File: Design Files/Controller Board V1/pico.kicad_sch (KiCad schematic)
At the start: 1 part, among them U5 SC0917

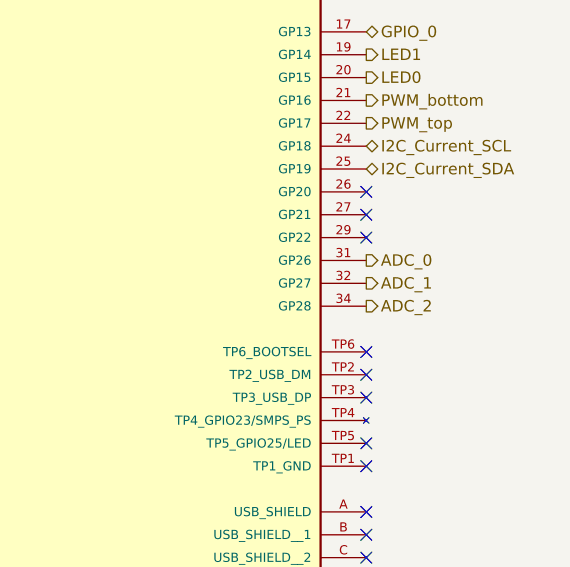
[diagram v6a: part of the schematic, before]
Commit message: current sensor done
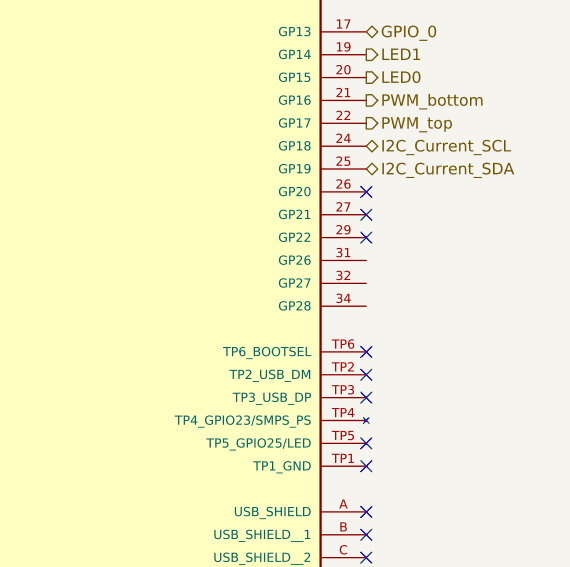
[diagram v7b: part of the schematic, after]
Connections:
- net ADC_0: no longer names the net of U5.31 (GP26)
- net ADC_1: no longer names the net of U5.32 (GP27)
- net ADC_2: no longer names the net of U5.34 (GP28)
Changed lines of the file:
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@@
 		(shape bidirectional)
 		(at 107.95 81.28 180)
-		(fields_autoplaced yes)
 		(effects
 			(font
@@
 		(shape bidirectional)
 		(at 107.95 91.44 180)
-		(fields_autoplaced yes)
-		(effects
-			(font
-				(size 1.27 1.27)
-			)
-			(justify right)
-		)
-	)
-	(hierarchical_label "ADC_1"
-		(shape output)
-		(at 158.75 96.52 0)
-		(fields_autoplaced yes)
-		(effects
-			(font
-				(size 1.27 1.27)
-			)
-			(justify left)
+		(effects
+			(font
+				(size 1.27 1.27)
+			)
+			(justify right)
 		)
 	)
@@
 		(shape bidirectional)
 		(at 107.95 78.74 180)
-		(fields_autoplaced yes)
 		(effects
 			(font
@@
 		(shape output)
 		(at 158.75 76.2 0)
-		(fields_autoplaced yes)
 		(effects
 			(font
@@
 		(shape input)
 		(at 88.9 53.34 180)
-		(fields_autoplaced yes)
 		(effects
 			(font
@@
 		(shape input)
 		(at 88.9 44.45 180)
-		(fields_autoplaced yes)
 		(effects
 			(font
@@
 		(shape output)
 		(at 107.95 83.82 180)
-		(fields_autoplaced yes)
 		(effects
 			(font
@@
 		(shape output)
 		(at 107.95 73.66 180)
-		(fields_autoplaced yes)
 		(effects
 			(font
@@
 		(shape output)
 		(at 107.95 93.98 180)
-		(fields_autoplaced yes)
 		(effects
 			(font
@@
 		(shape output)
 		(at 158.75 73.66 0)
-		(fields_autoplaced yes)
 		(effects
 			(font
@@
 		(shape output)
 		(at 158.75 53.34 0)
-		(fields_autoplaced yes)
 		(effects
 			(font
@@
 		(shape input)
 		(at 107.95 68.58 180)
-		(fields_autoplaced yes)
 		(effects
 			(font
@@
 		(shape bidirectional)
 		(at 158.75 68.58 0)
-		(fields_autoplaced yes)
 		(effects
 			(font
@@
 		(shape bidirectional)
 		(at 158.75 81.28 0)
-		(fields_autoplaced yes)
-		(effects
-			(font
-				(size 1.27 1.27)
-			)
-			(justify left)
-		)
-	)
-	(hierarchical_label "ADC_0"
-		(shape output)
-		(at 158.75 93.98 0)
-		(fields_autoplaced yes)
 		(effects
 			(font
@@
 		(shape bidirectional)
 		(at 107.95 88.9 180)
-		(fields_autoplaced yes)
 		(effects
 			(font
@@
 		(shape input)
 		(at 107.95 71.12 180)
-		(fields_autoplaced yes)
-		(effects
-			(font
-				(size 1.27 1.27)
-			)
-			(justify right)
-		)
-	)
-	(hierarchical_label "ADC_2"
-		(shape output)
-		(at 158.75 99.06 0)
-		(fields_autoplaced yes)
-		(effects
-			(font
-				(size 1.27 1.27)
-			)
-			(justify left)
+		(effects
+			(font
+				(size 1.27 1.27)
+			)
+			(justify right)
 		)
 	)
@@
 		(shape output)
 		(at 107.95 86.36 180)
-		(fields_autoplaced yes)
 		(effects
 			(font
@@
 		(shape bidirectional)
 		(at 158.75 83.82 0)
-		(fields_autoplaced yes)
 		(effects
 			(font
@@
 		(shape input)
 		(at 158.75 50.8 0)
-		(fields_autoplaced yes)
 		(effects
 			(font
@@
 		(shape bidirectional)
 		(at 107.95 99.06 180)
-		(fields_autoplaced yes)
 		(effects
 			(font
@@
 		(shape output)
 		(at 107.95 76.2 180)
-		(fields_autoplaced yes)
 		(effects
 			(font
@@
 		(shape output)
 		(at 158.75 78.74 0)
-		(fields_autoplaced yes)
 		(effects
 			(font
@@
 		(shape input)
 		(at 88.9 49.53 180)
-		(fields_autoplaced yes)
 		(effects
 			(font
@@
 		(shape output)
 		(at 158.75 71.12 0)
-		(fields_autoplaced yes)
 		(effects
 			(font
@@
 		(shape output)
 		(at 107.95 96.52 180)
-		(fields_autoplaced yes)
-		(effects
-			(font
+		(effects
+			(font

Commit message: Minor Changes
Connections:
- net GNDA renamed A_GND
- net GNDD renamed D_GND
- no-connect marks 18 -> 21
